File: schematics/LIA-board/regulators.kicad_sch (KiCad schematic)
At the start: 36 parts, among them U1 LMR51430, U18 LMR51430, U20 ADP7118ACPZN, U3 LT3094xMSE, U4 ADP7118ACPZN, U5 ADP7118ACPZN

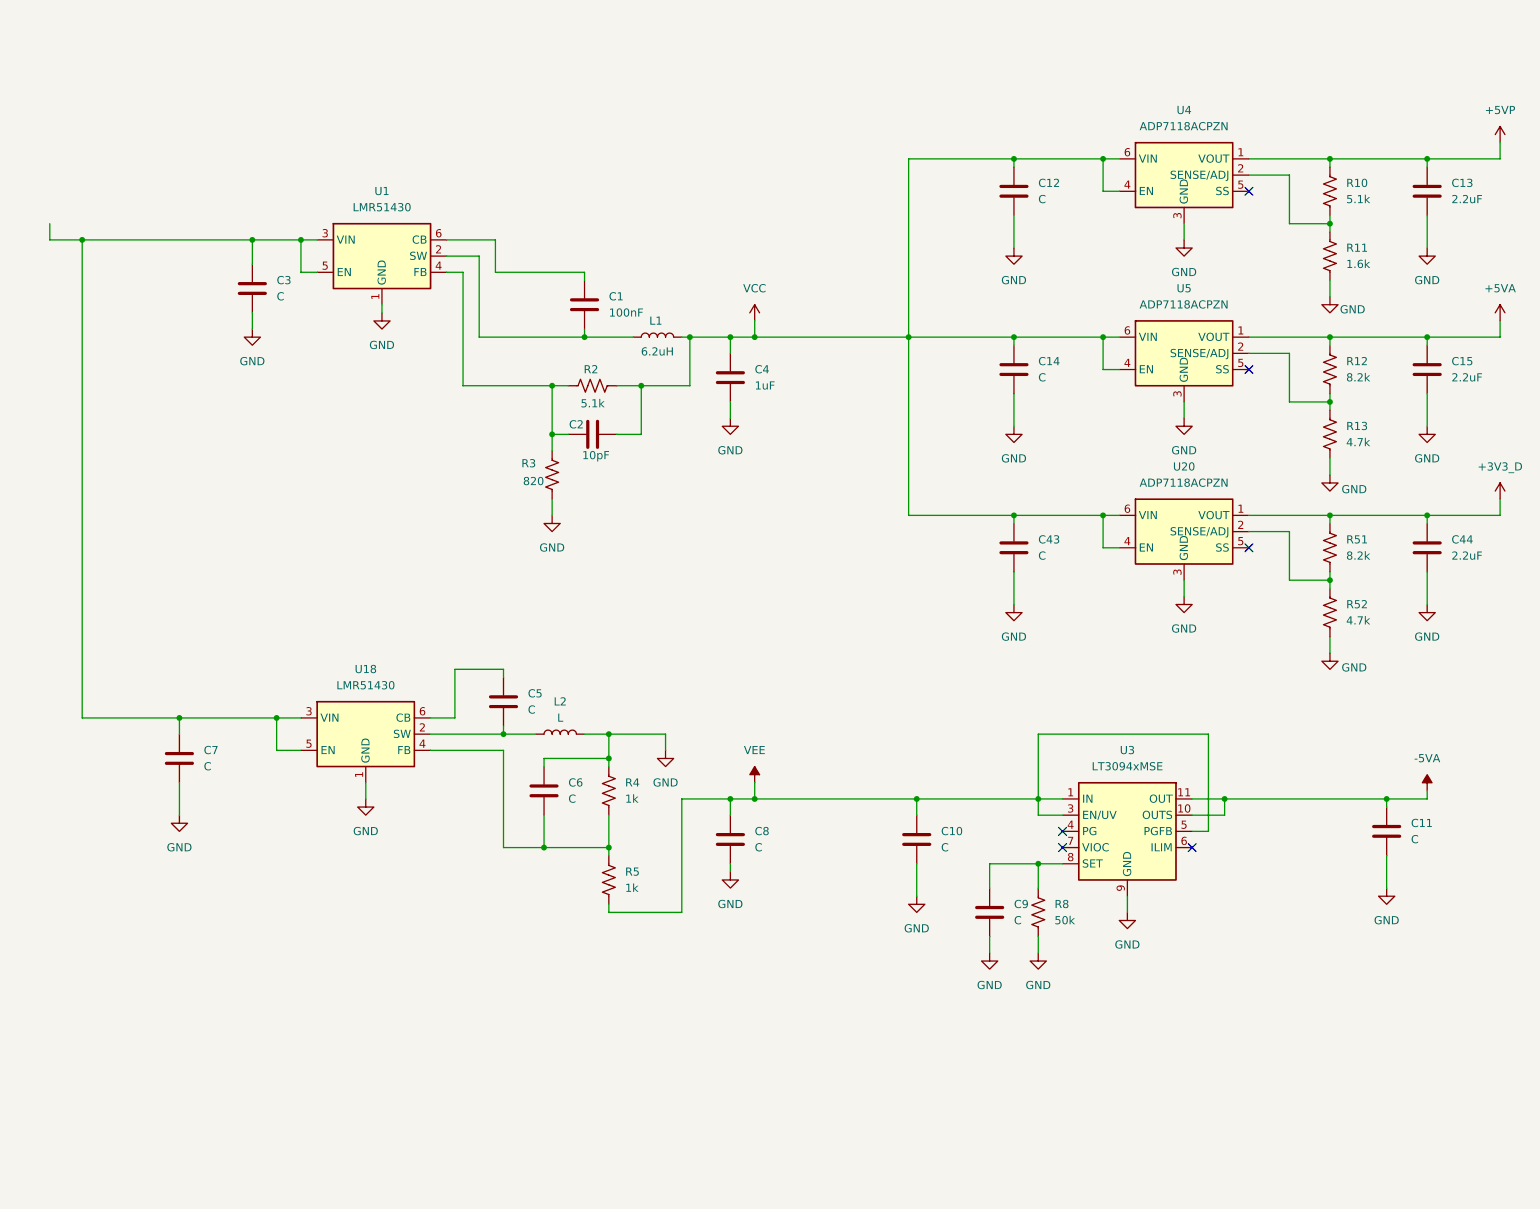
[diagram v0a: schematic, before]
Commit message: commit before changing the oscillator implementation
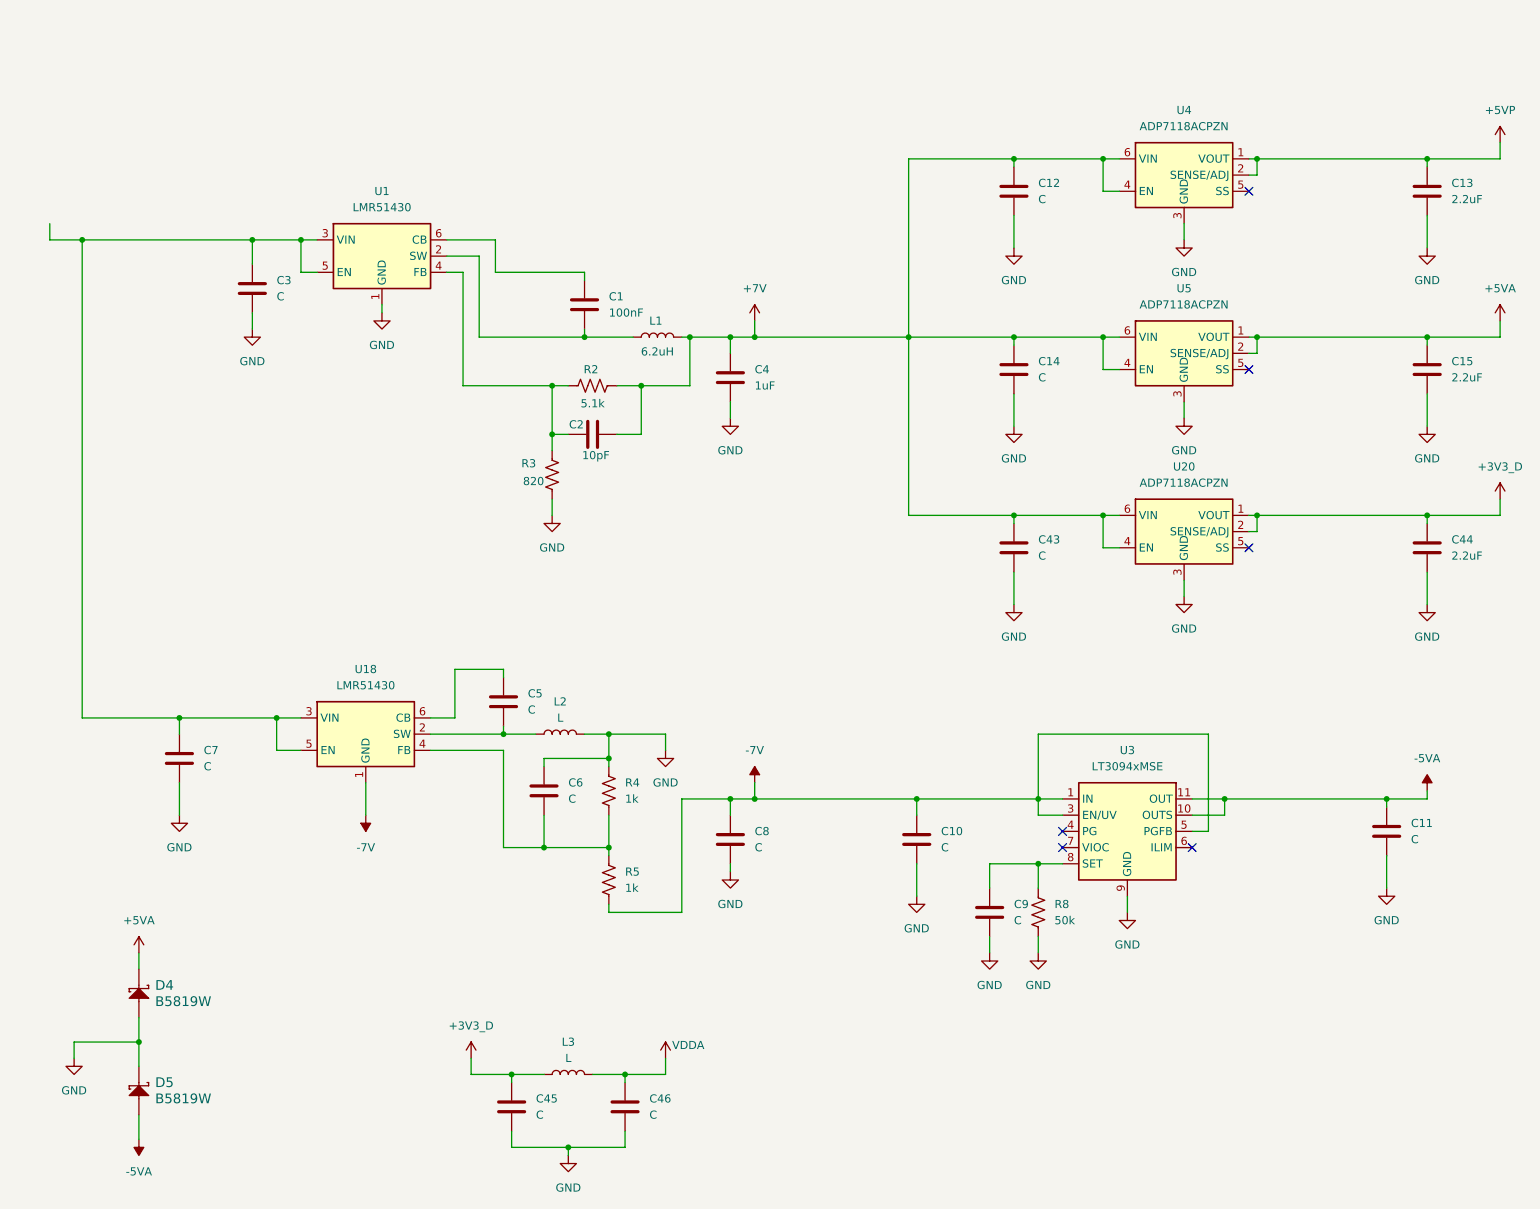
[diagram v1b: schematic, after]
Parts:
- removed R10: 5.1k, SparkFun-Resistor:R_0603_1608Metric, symbol SparkFun:R
- removed R11: 1.6k, SparkFun-Resistor:R_0603_1608Metric, symbol SparkFun:R
- removed R12, R51: 8.2k, SparkFun-Resistor:R_0603_1608Metric, symbol SparkFun:R
- removed R13, R52: 4.7k, SparkFun-Resistor:R_0603_1608Metric, symbol SparkFun:R
- added C45, C46: C, SparkFun-Resistor:R_0603_1608Metric, symbol Device:C
- added D4, D5: B5819W, symbol CERN:Diode Schottky
- added L3: L, symbol Device:L
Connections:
- net +3V3_D: now also U20.2 (SENSE/ADJ), C45.1, L3.1
- net +5VA: now also U5.2 (SENSE/ADJ), D4.1 (C)
- net +5VP: now also U4.2 (SENSE/ADJ)
- net -5VA: now also D5.2 (A)
- net GND: now also C45.2, C46.2, D4.2 (A), D5.1 (C); no longer U18.1 (GND)
- net VCC renamed +7V
- net VEE renamed -7V
- net -7V: now also U18.1 (GND)
- new net VDDA: C46.1, L3.2

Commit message: commit before changing LIA
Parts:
- added C50: C, SparkFun-Resistor:R_0603_1608Metric, symbol Device:C
- added C51: 2.2uF, SparkFun-Resistor:R_0603_1608Metric, symbol Device:C
- added U22: ADP7118ACPZN, Package_CSP:LFCSP-6-1EP_2x2mm_P0.65mm_EP1x1.6mm, symbol Regulator_Linear:ADP7118ACPZN
- renumbered C12 to C27, C13 to C28, C3 to C29, C1 to C30, C14 to C31, C15 to C32, C4 to C33, C2 to C34, C43 to C35, C44 to C36, C5 to C37, C7 to C38, C6 to C39, C11 to C40, C8 to C41, C10 to C42, C9 to C43, C45 to C44, C46 to C45, D4 to D1, D5 to D2, R2 to R33, R3 to R34, R4 to R35, R5 to R36, R8 to R37, U4 to U14, U1 to U15, U5 to U16, U20 to U17, U3 to U19
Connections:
- net Vin: now reaches C29.1, C38.1, U15.3 (VIN), U15.5 (EN), U18.3 (VIN), U18.5 (EN)
- new net 3V3_iso: C51.1, U22.1 (VOUT), U22.2 (SENSE/ADJ)
- new net 5V_FTDI: C50.1, U22.4 (EN), U22.6 (VIN)
- new net FTDI_gnd: C50.2, C51.2, U22.3 (GND), U22.7 (GND)
- no-connect marks 6 -> 7
